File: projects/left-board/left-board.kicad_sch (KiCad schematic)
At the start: 6 parts, among them J1 5051101292, SW1 TS06-667-25-BK-160-G-SMT-TR, SW2 TS06-667-25-BK-160-G-SMT-TR, SW3 TS06-667-25-BK-160-G-SMT-TR, SW4 TS06-667-25-BK-160-G-SMT-TR, SW5 TS06-667-25-BK-160-G-SMT-TR

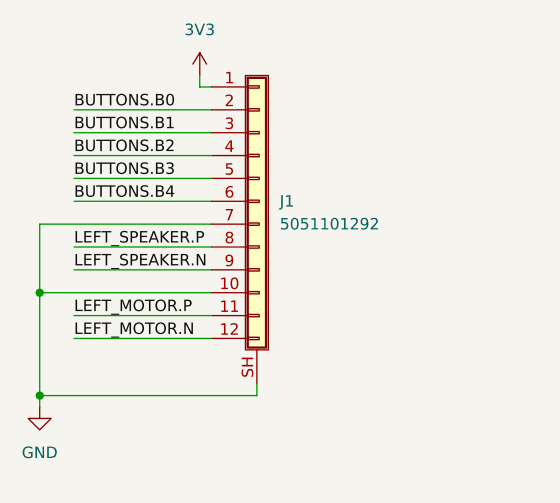
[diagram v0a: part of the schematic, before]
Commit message: Fix wrong net name on left audio
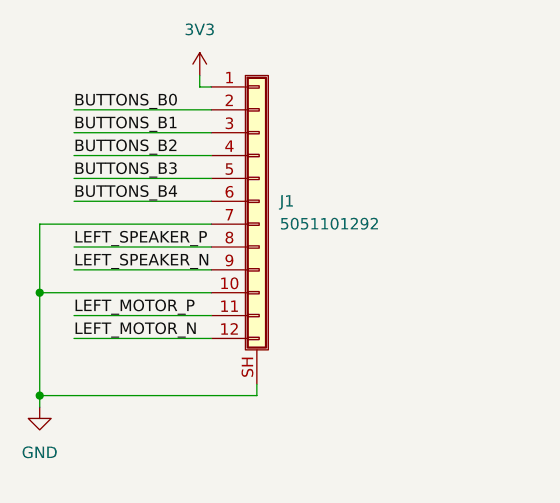
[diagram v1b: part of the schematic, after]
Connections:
- net BUTTONS.B0 is gone; now on net BUTTONS_B0: J1.2 (Pin_2)
- net BUTTONS.B1 is gone; now on net BUTTONS_B1: J1.3 (Pin_3)
- net BUTTONS.B2 is gone; now on net BUTTONS_B2: J1.4 (Pin_4)
- net BUTTONS.B3 is gone; now on net BUTTONS_B3: J1.5 (Pin_5)
- net BUTTONS.B4 is gone; now on net BUTTONS_B4: J1.6 (Pin_6)
- net LEFT_MOTOR.N renamed LEFT_MOTOR_N
- net LEFT_MOTOR.P renamed LEFT_MOTOR_P
- net LEFT_SPEAKER.N renamed LEFT_SPEAKER_N
- net LEFT_SPEAKER.P renamed LEFT_SPEAKER_P
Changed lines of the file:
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@@
 		)
 	)
-	(label "LEFT_MOTOR.P"
+	(label "LEFT_MOTOR_P"
 		(at 105.41 64.77 0)
 		(effects
@@
 		)
 	)
-	(label "BUTTONS.B1"
+	(label "BUTTONS_B1"
 		(at 105.41 44.45 0)
 		(effects
@@
 		)
 	)
-	(label "LEFT_MOTOR.N"
+	(label "LEFT_MOTOR_N"
 		(at 105.41 67.31 0)
 		(effects
@@
 		)
 	)
-	(label "BUTTONS.B0"
+	(label "BUTTONS_B0"
 		(at 105.41 41.91 0)
 		(effects
@@
 		)
 	)
-	(label "BUTTONS.B3"
+	(label "BUTTONS_B3"
 		(at 105.41 49.53 0)
 		(effects
@@
 		)
 	)
-	(label "BUTTONS.B4"
+	(label "BUTTONS_B4"
 		(at 105.41 52.07 0)
 		(effects
@@
 		)
 	)
-	(label "LEFT_SPEAKER.P"
+	(label "LEFT_SPEAKER_P"
 		(at 105.41 57.15 0)
 		(effects
@@
 		)
 	)
-	(label "BUTTONS.B2"
+	(label "BUTTONS_B2"
 		(at 105.41 46.99 0)
 		(effects
@@
 		)
 	)
-	(label "LEFT_SPEAKER.N"
+	(label "LEFT_SPEAKER_N"
 		(at 105.41 59.69 0)
 		(effects
